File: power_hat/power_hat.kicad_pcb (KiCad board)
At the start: 4 copper layers, 47.1 x 127.1 mm, 56 parts, among them IC1 TPS259830LNRGER, J1 XT30PW-M/Terminal block, J10 XT30PW-M/Terminal block, J11 XT30PW-M/Terminal block, J12 XT30PW-M/Terminal block, J2 XT30PW-M/Terminal block, J3 XT30PW-M/Terminal block, J4 XT30PW-M/Terminal block, J5 Conn_01x02_Pin, J6 XT30PW-M/Terminal block, J7 Conn_01x02_Pin, J8 XT30PW-M/Terminal block, J9 XT30PW-M/Terminal block, Q1 CSD18540Q5B, Q4 SQJ461EP-T1_GE3, Q5 SQJ461EP-T1_GE3, U17 ADM1270ARQZ

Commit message: added power changes
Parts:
- removed R30: 80k6, Resistor_SMD:R_0805_2012Metric
- removed R31: 100k, Resistor_SMD:R_0805_2012Metric
- C40: value 100nF - 50V X7R -> 2.2uF
- CdVdt1: value 0.018uF 630VDC 1% 1210 C0G (NP0) -> 0.1uF 630VDC 1% 1210 C0G (NP0)
- Citimer1: value 10nF -> 47nF
- D1: value SMCJ5.0A -> SMCJ28A
- R33: value 50m -> 5m
- moved C2 35.7 mm to (94.8, 66.5), turned to 90 degrees
- moved Cin4 32.0 mm to (98.3, 66.7), turned to 90 degrees
- moved D1 31.4 mm to (115.4, 29.7), turned to 180 degrees
- moved Q5 29.7 mm to (105.1, 70.2), turned to 90 degrees
- moved C40 25.7 mm to (99.1, 59.9), turned to 180 degrees
- moved R36 24.6 mm to (101.5, 62.3), turned to 180 degrees
- moved C41 24.5 mm to (99.1, 57.9), turned to 180 degrees
- moved R35 24.4 mm to (103.4, 64.3), turned to 180 degrees
- moved J5 24.1 mm to (118.6, 35.2), turned to 0 degrees
- moved JP1 23.7 mm to (126.7, 64.2), turned to -90 degrees
- moved Q1 23.4 mm to (125.0, 65.4), turned to -90 degrees
- moved R32 23.0 mm to (99.4, 55.0), turned to -90 degrees
- moved R29 22.5 mm to (99.5, 51.4), turned to 90 degrees
- moved R34 20.6 mm to (105.2, 62.3), turned to 180 degrees
- moved D2 19.1 mm to (112.2, 65.0), turned to 90 degrees
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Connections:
- U17 pad 4: Net-(U17-ISET) -> /VCAP
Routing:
- net Net-(U17-ISET): track 8.09 -> 0.00 mm, vias 2 -> 0
- net /VCAP: track 13.9 -> 10.1 mm
- net /route_+: track 8.04 -> 10.2 mm, vias 2 -> 6
- net /route_-: track 6.63 -> 7.27 mm
- net GND: vias 114 -> 104
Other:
- board size 47.1 x 127.1 mm -> 47.1 x 133.6 mm
- board text removed: "CHARGE DONE"
- board text removed: "CHARGE IN PROGRESS"
- board text removed: "LEFT"
- board text removed: "PASSIVATE BATTERY"
- board text removed: "RBF_BAT"
- board text removed: "RBF_TRIG"
- board text removed: "RIGHT"
- board text removed: "RS-,RS+,CAN+,CAN-,GND,24_SAT GND,GND,GND,GND,GND,GND"

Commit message: added gerbers and final modifications before ordering
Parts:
- Cin2, Cin3: value T543X106K063AHW050 -> T521D106M050ATE120; footprint lib_fp:T543X106K063AHW050 -> lib_fp:T521D
- moved Cin3 0.83 mm to (108.9, 41.3)
- moved Cin2 0.76 mm to (123.9, 42.5)
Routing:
- net /route_+: track 10.2 -> 9.66 mm

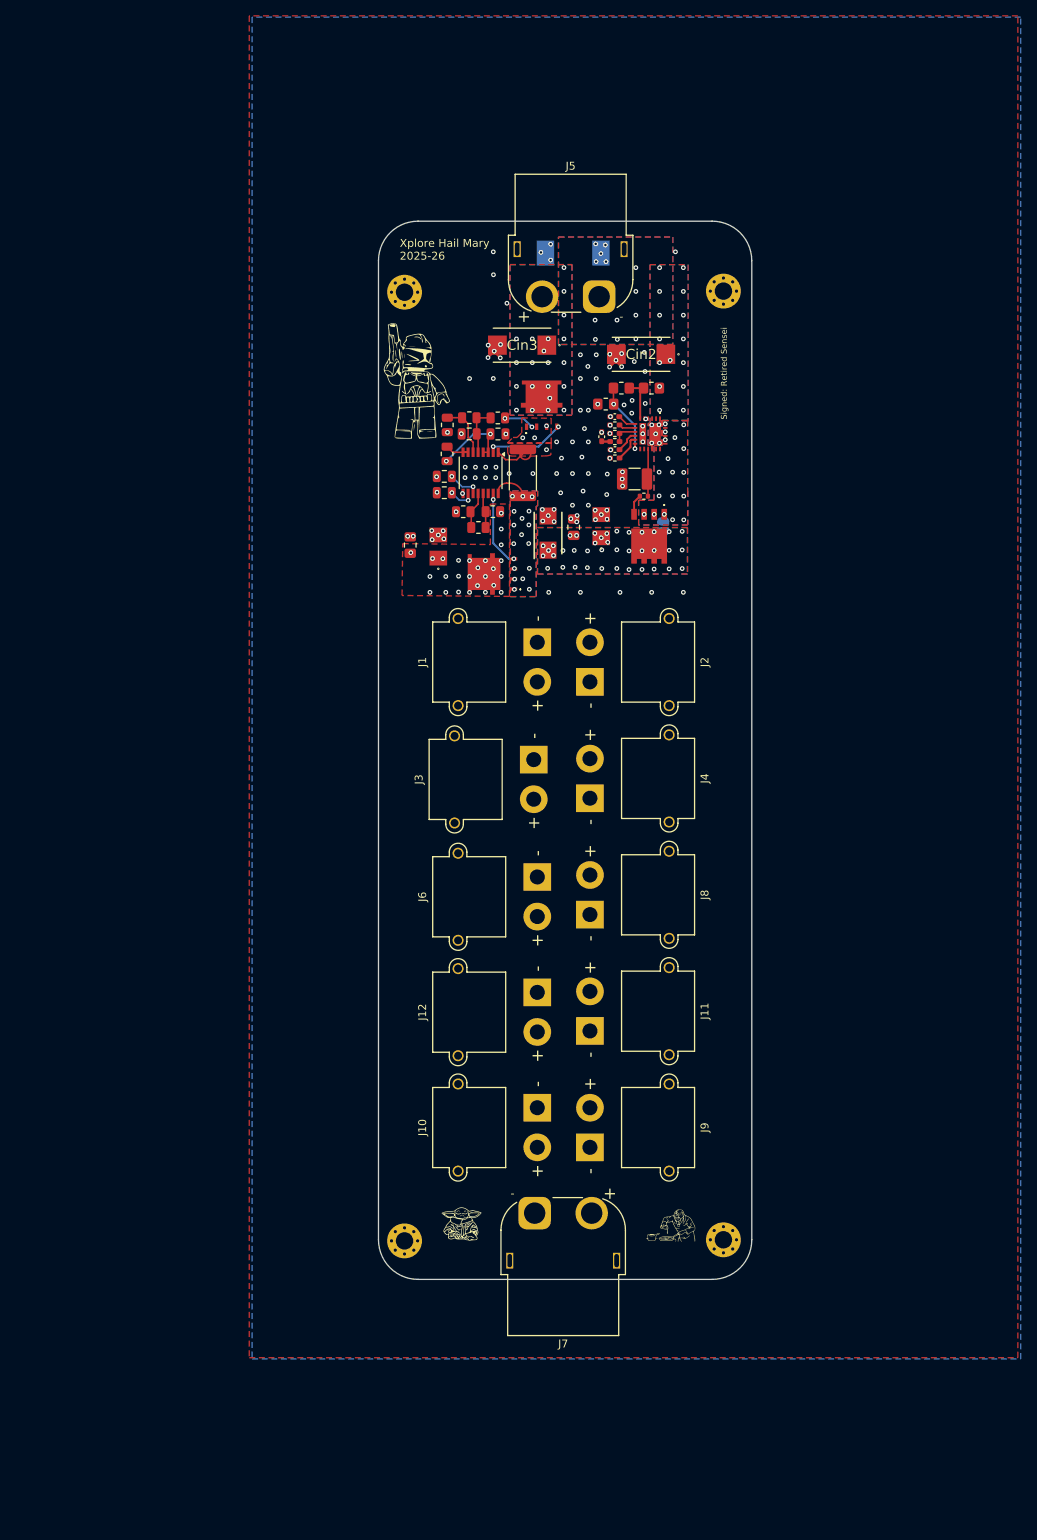
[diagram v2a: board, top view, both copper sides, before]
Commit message: added monitoring, rerouting partially
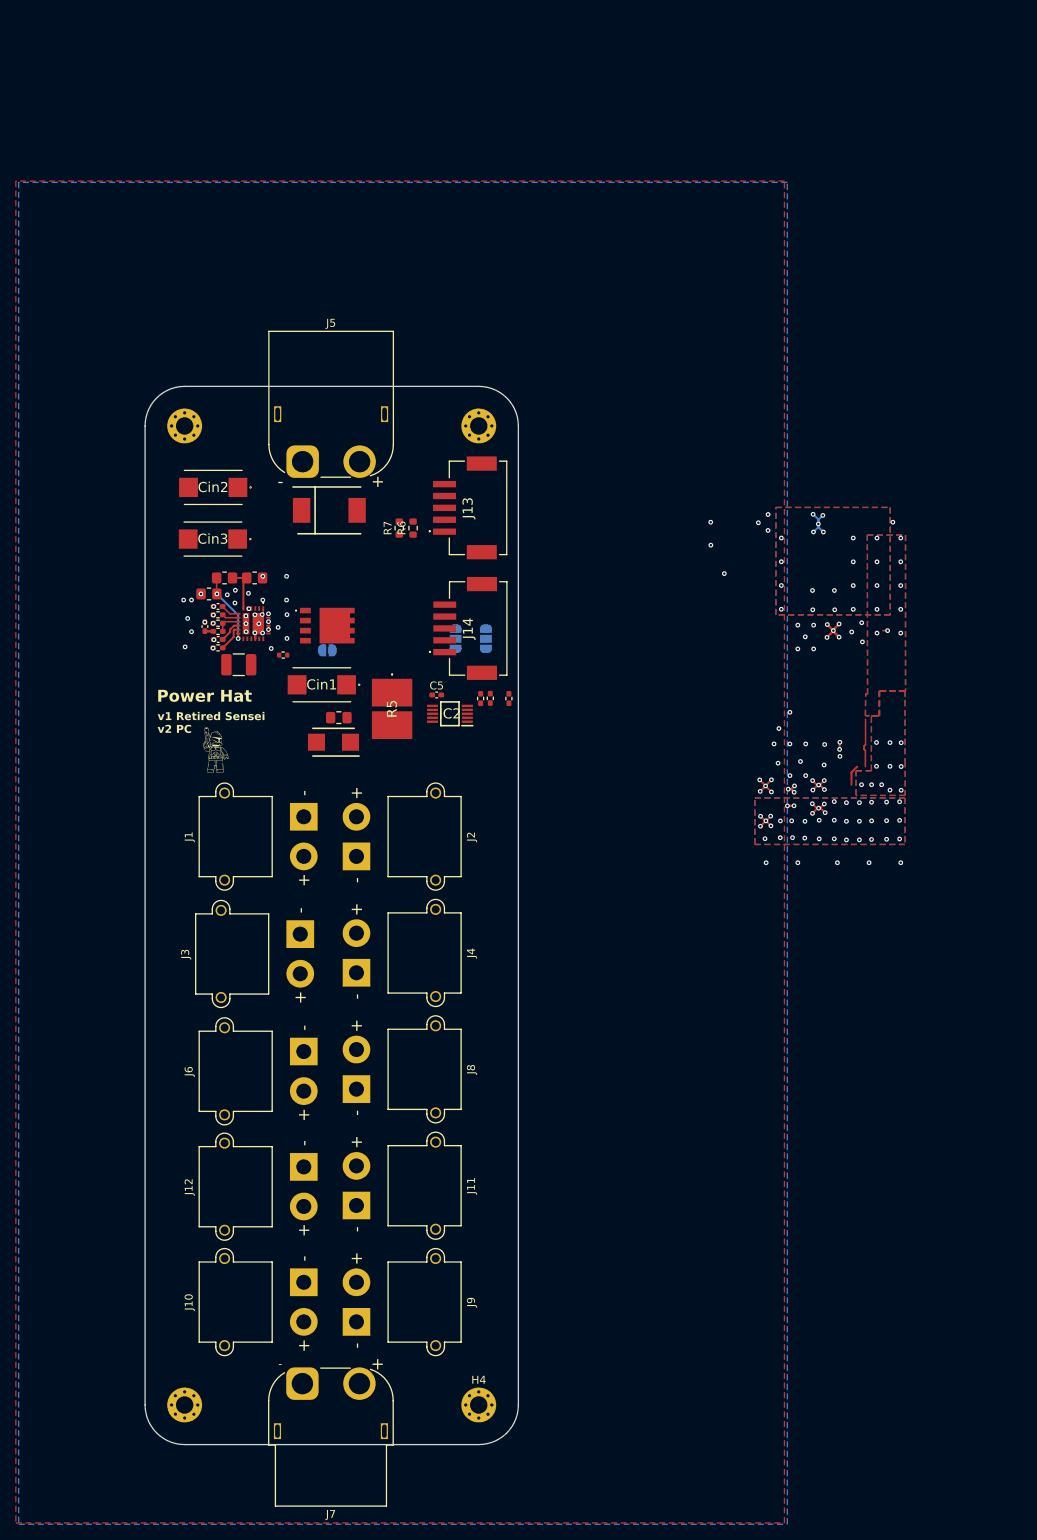
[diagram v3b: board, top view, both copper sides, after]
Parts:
- removed C2: 1uF, Capacitor_SMD:C_0805_2012Metric_Pad1.18x1.45mm_HandSolder
- removed C38: 1uF - 50V X7R, Capacitor_SMD:C_0805_2012Metric
- removed C39: 1nF - 50V X7R, Capacitor_SMD:C_0805_2012Metric
- removed C40: 2.2uF, Capacitor_SMD:C_0805_2012Metric
- removed C41: 100nF - 50V X7R, Capacitor_SMD:C_0805_2012Metric
- removed Cin4: T521D475M063ATE075, lib_fp:T520B
- removed the H3 at (134.3, 34.5)
- removed the H3 at (134.3, 154.3)
- removed the H4 at (94.1, 34.6)
- removed the H4 at (94.1, 154.4)
- removed Q4, Q5: SQJ461EP-T1_GE3, lib_fp:SQJ461EPT1_GE3
- removed R27, R28, R29: NOTE, Resistor_SMD:R_0805_2012Metric
- removed R32: 10k, Resistor_SMD:R_0805_2012Metric
- removed R33: 5m, Resistor_SMD:R_2512_6332Metric
- removed R34: 90k9, Resistor_SMD:R_0805_2012Metric
- removed R35: 174, Resistor_SMD:R_0805_2012Metric
- removed R36: 4k, Resistor_SMD:R_0805_2012Metric
- removed U17: ADM1270ARQZ, Package_SO:SSOP-16_3.9x4.9mm_P0.635mm
- added C5: 0.1uF, Capacitor_SMD:C_0402_1005Metric_Pad0.74x0.62mm_HandSolder, F.Cu at (98.1, 85.5)
- added H1: M2, MountingHole:MountingHole_2.2mm_M2_Pad_Via, F.Cu at (103.4, 51.5)
- added H2: M2, MountingHole:MountingHole_2.2mm_M2_Pad_Via, F.Cu at (66.3, 175.1)
- added H3: M2, MountingHole:MountingHole_2.2mm_M2_Pad_Via, F.Cu at (66.3, 51.5)
- added H4: M2, MountingHole:MountingHole_2.2mm_M2_Pad_Via, F.Cu at (103.4, 175.1)
- added IC2: INA238AQDGSRQ1, xt60:SOP50P490X110-10N, F.Cu at (99.8, 87.8)
- added J13: 502585-0570, lib_fp:5025850570, F.Cu at (103.0, 61.8)
- added J14: 502585-0570, lib_fp:5025850570, F.Cu at (103.1, 77.1)
- added JP2: ~, Jumper:SolderJumper-3_P1.3mm_Open_RoundedPad1.0x1.5mm, B.Cu at (100.5, 78.4)
- added JP3: ~, Jumper:SolderJumper-3_P1.3mm_Open_RoundedPad1.0x1.5mm, B.Cu at (104.3, 78.4)
- added R10: 10k, Resistor_SMD:R_0402_1005Metric_Pad0.72x0.64mm_HandSolder, F.Cu at (107.2, 85.9)
- added R11: 10k, Resistor_SMD:R_0402_1005Metric_Pad0.72x0.64mm_HandSolder, F.Cu at (104.9, 85.9)
- added R12: 10k, Resistor_SMD:R_0402_1005Metric_Pad0.72x0.64mm_HandSolder, F.Cu at (103.7, 85.9)
- added R5: WSHM28188L000FEA, lib_fp:WSHM28188L000FEA, F.Cu at (92.5, 87.2)
- added R6: R, Resistor_SMD:R_0603_1608Metric, F.Cu at (95.2, 64.4)
- added R7: R, Resistor_SMD:R_0603_1608Metric, F.Cu at (93.4, 64.4)
- Cin1: footprint lib_fp:T520B -> lib_fp:T521D
- D1: moved to F.Cu
- J5: footprint Connector_AMASS:AMASS_XT60PW-F_1x02_P7.20mm_Horizontal -> Connector_AMASS:AMASS_XT60PW-M_1x02_P7.20mm_Horizontal
- moved Cin2 56.6 mm to (69.9, 59.3)
- moved C_{imon_filter}1 55.5 mm to (68.9, 76.8)
- moved Citimer1 55.5 mm to (70.5, 74.3)
- moved IC1 55.5 mm to (75.0, 76.5)
- moved R1 55.5 mm to (75.1, 70.7)
- moved R2 55.5 mm to (71.3, 70.7)
- moved R3 55.5 mm to (69.4, 72.7)
- moved R4 55.5 mm to (70.5, 79.5)
- moved R_{imon_filter}1 55.5 mm to (70.5, 77.4)
- moved Rillim1 55.5 mm to (70.5, 75.3)
- moved Rimon1 55.5 mm to (70.5, 76.4)
- moved Cretry_dly1 55.5 mm to (70.5, 78.5)
- moved CdVdt1 55.2 mm to (73.1, 81.7)
- moved RG1 49.8 mm to (78.8, 80.4), turned to 180 degrees
- moved Cin3 46.1 mm to (69.9, 65.8)
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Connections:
- C1 pad 1: VCC -> /VOUT
- Cin1 pad 1: VCC -> /VOUT
- JP1 pad 2: VCC -> /VOUT
- Q1 pad 5: VCC -> /VOUT
- Q1 pad 6: VCC -> /VOUT
- Q1 pad 7: VCC -> /VOUT
- Q1 pad 8: VCC -> /VOUT
- Q1 pad 9: VCC -> /VOUT
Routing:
- net Net-(Q4-G): track 10.2 -> 0.00 mm, vias 2 -> 0
- net /VCAP: track 10.1 -> 0.00 mm, vias 2 -> 0
- net Net-(Q5-G): track 9.73 -> 0.00 mm, vias 2 -> 0
- net /route_+: track 9.66 -> 0.00 mm, vias 6 -> 0
- net GND: track 25.2 -> 16.5 mm, vias 104 -> 72
- net /route_-: track 7.27 -> 0.00 mm, vias 17 -> 0
- net Net-(U17-OV): track 6.80 -> 0.00 mm
- net Net-(U17-UV): track 6.23 -> 0.00 mm
- net Net-(U17-FB_PG): track 4.74 -> 0.00 mm
- net Net-(U17-FLB): track 4.43 -> 0.00 mm
- net Net-(U17-eTIMER_OFF): track 4.07 -> 0.00 mm, vias 2 -> 0
- net Net-(U17-*FAULT): track 3.58 -> 0.00 mm
- net Net-(U17-TIMER): track 3.33 -> 0.00 mm, vias 2 -> 0
- net VCC: track 8.78 -> 8.53 mm, vias 65 -> 39
- net EFUSE: track 11.5 -> 11.3 mm, vias 54 -> 37
- removed copper zone on F.Cu, net /route_+
- removed copper zone on B.Cu, net /route_-
- removed copper zone on F.Cu, net /route_-
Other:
- board text added: "Power Hat"
- board text added: "v1 Retired Sensei v2 PC"
- board text removed: "I am the Empire"
- board text removed: "Signed: Retired Sensei"
- board text removed: "Xplore Hail Mary 2025-26"
